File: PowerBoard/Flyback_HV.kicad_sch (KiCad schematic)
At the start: 43 parts, among them J3 Molex Microfit 3.0, Q2 FDD86250-F085, Q3 FGH75T65SQD-F155, T1 DA2034, U2 LT3750, U4 MCP14A0454-E/SN

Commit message: auto discharge circuit
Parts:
- removed D1: D, bots:D_SMB, symbol Device:D
- removed D3 (x2): D_Schottky, bots:D_SMC, symbol Device:D_Schottky
- removed D4 (x2): D_Zener, bots:D_SMA, symbol Device:D_Zener
- removed Q3 (x2): FGH75T65SQD-F155, bots:TO-247-3_Horizontal_TabDown, symbol Transistor_IGBT:IRG4PF50W
- added C1: 0.1u, bots:C_1210_3225Metric, symbol Device:C
- added D1, D10: SMAJ14A, bots:D_SMA, symbol bots:SMAJ14A
- added D11, D2: MUR860J, bots:D_SMC, symbol bots:MUR860J
- added D12: 3SMBJ5929B-TP, bots:D_SMB, symbol bots:D_ZENER_3SMBJ5929B-TP
- added D3: D_Schottky, bots:D_SMB, symbol Device:D_Schottky
- added Q3, Q7: FGH50T65SQD-F155, bots:TO-247-3_Horizontal_TabDown, symbol bots:FGH50T65SQD-F155
- added Q5: TN2130K1-G, BSS138:SOT95P240X111-3N, symbol bots:TN2130K1-G
- added Q6: STD11N60DM2, bots:DPAK-3_ONS, symbol bots:STD11N60DM2
- added R44: 1k 50W, bots:TO-263-2, symbol bots:1k 50W
- added R9: 100k, bots:R_0603_1608Metric, symbol Device:R
- added R9: 270k, bots:R_0603_1608Metric, symbol Device:R
- added R9 (x2): 5.1M, bots:R_0603_1608Metric, symbol Device:R
- added TP19: DONE, bots:TestPoint_Pad_1.0x1.0mm, symbol Connector:TestPoint
- added TP20: CHARGE, bots:TestPoint_Pad_1.0x1.0mm, symbol Connector:TestPoint
- added TP21: VGATE, bots:TestPoint_Pad_1.0x1.0mm, symbol Connector:TestPoint
- added TP22: GATEB, bots:TestPoint_Pad_1.0x1.0mm, symbol Connector:TestPoint
- added TP23: CHICKER_GATE, bots:TestPoint_Pad_1.0x1.0mm, symbol Connector:TestPoint
- added TP24: CHIP, bots:TestPoint_Pad_1.0x1.0mm, symbol Connector:TestPoint
- added TP25: CHICK, bots:TestPoint_Pad_1.0x1.0mm, symbol Connector:TestPoint
- U4: footprint bots:SOIC-8_3.9x4.9mm_P1.27mm -> SOIC8_SN_MCH
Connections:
- net CHARGE: now also TP20.1
- net CHICKER: now also TP25.1
- net CHICKER_GATE: now also TP23.1
- net CHICKER_HV: now also D11.2 (A), Q3.2 (C)
- net CHIP_EXTRA: now also TP24.1
- net DONE: now also TP19.1
- net EXTRA_GATE: now also TP22.1
- net EXTRA_HV: now also D2.2 (A), Q7.2 (C)
- net GNDPWR: now also C1.2, D1.2 (A), D10.2 (A), D12.2 (A), Q3.3 (E), Q5.2, Q6.3 (S), Q7.3 (E), R44.2, R9.2
- net HV: now also C1.1, D11.1 (K), D2.1 (K), D3.1 (K), R44.1, R9.1
- net HV_DIO: now also D3.2 (A)
- net IGBTGATE_CHICKER: now also D1.1 (K), Q3.1 (G)
- net IGBTGATE_EXTRA: now also D10.1 (K), Q7.1 (G)
- net VCC: now also R9.1
- net at Q2.1 (G), U2.7 (GATE): now also TP21.1
- new net AD_50W: Q6.2 (D), R44.3
- new net AD_G: D12.1 (K), Q5.3, Q6.1 (G), R9.2
- new net AD_LV_G: Q5.1, R9.1, R9.2
- new net AD_R: R9.1, R9.2
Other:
- note added: "Vth = 2.4V, at lowest 14.8 roughly this is still at 4V. So only when it is disconnected will it not be tied to ground"
- note removed: "4775.207283"
- note removed: "4797.333031"
- note removed: "7087.375394"
- moved on the sheet: C5, C6, D2, R6, R7, R8

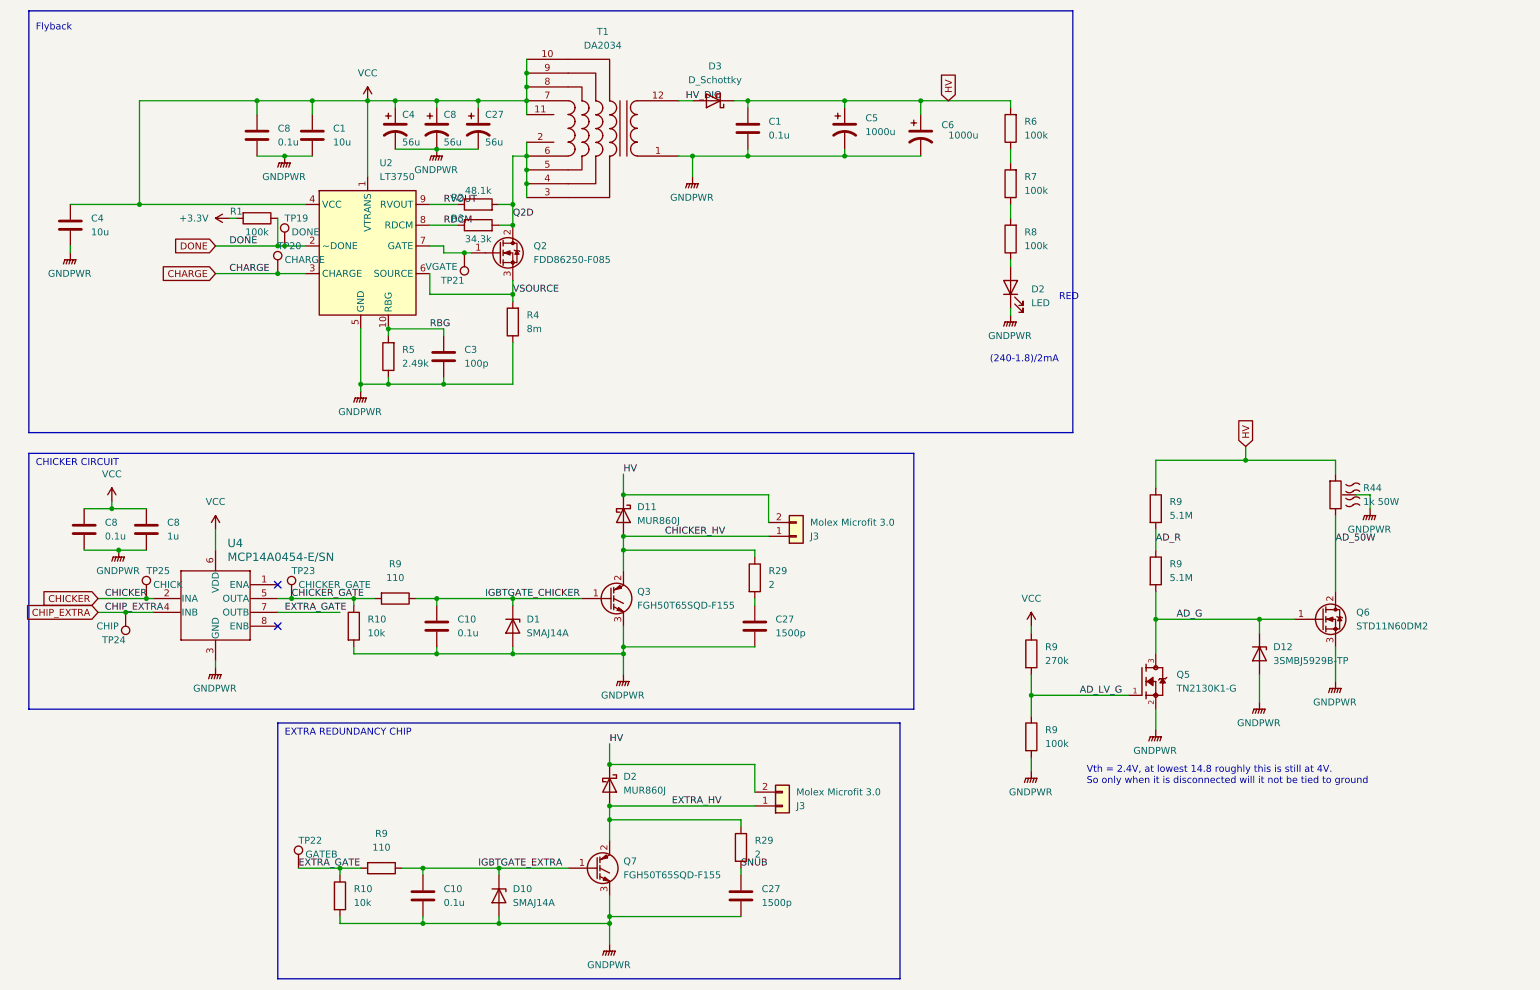
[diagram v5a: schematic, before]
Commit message: updated board edge clearance and cap model
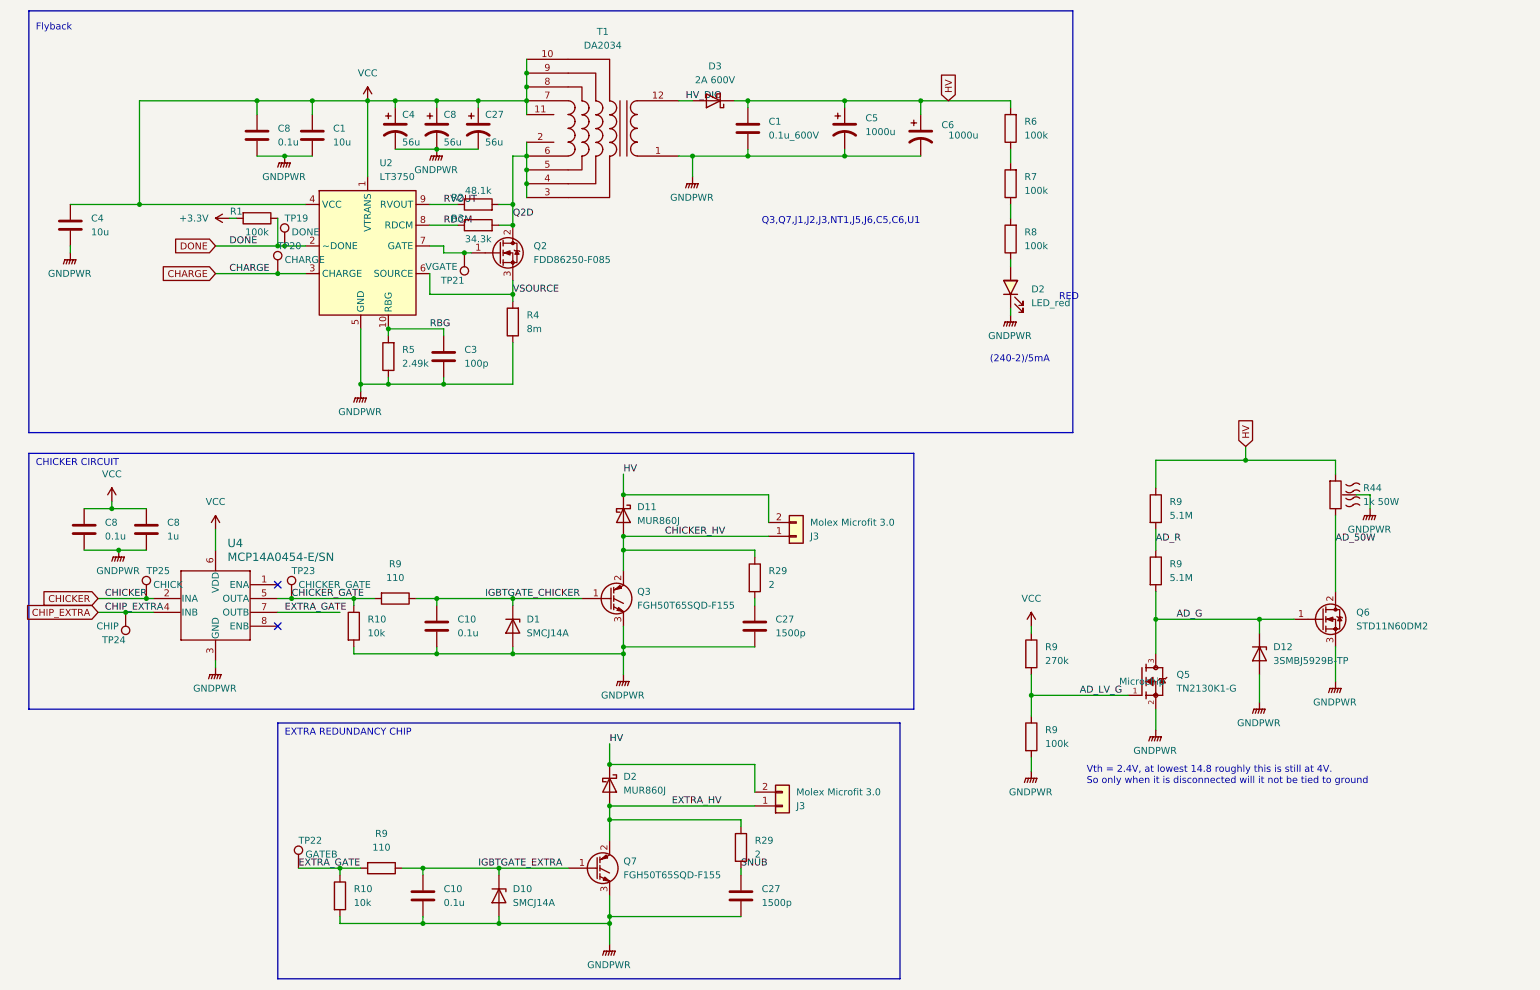
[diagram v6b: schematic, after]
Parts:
- removed D1, D10: SMAJ14A, bots:D_SMA, symbol bots:SMAJ14A
- added D1, D10: SMCJ14A, bots:D_SMC, symbol bots:SMCJ14A
- C1, C4: symbol Device:C -> bots:C_10u; JLC (none) -> 0805; LCSC (none) -> C440198; MPN (none) -> GRM21BR61H106KE43L; Manufacturer (none) -> Murata; Price (none) -> 0.0645
- C1: value 0.1u -> 0.1u_600V; symbol Device:C -> bots:C_0.1u_600V; JLC (none) -> 1210; LCSC (none) -> C342668; MPN (none) -> C3225X7T2J104KT000N; Manufacturer (none) -> TDK; Price (none) -> 0.3623
- C10, C8: symbol Device:C -> bots:C_0.1u; JLC (none) -> 0603; LCSC (none) -> C14663; MPN (none) -> CC0603KRX7R9BB104; Manufacturer (none) -> YAGEO; Price (none) -> 0.0021
- C27: symbol Device:C -> bots:C_1500p; JLC (none) -> 0805; LCSC (none) -> C342996; MPN (none) -> C2012C0G2A152JT000N; Manufacturer (none) -> TDK; Price (none) -> 0.0396
- C27, C4, C8: symbol bots:CAP_A768EB566M1VLAE042 -> bots:CAP_56uPOL; MPN (none) -> UWD1V560MCL1GS; Manufacturer (none) -> Nichion; Price (none) -> 0.79
- C3: symbol Device:C -> bots:C_100p; JLC (none) -> 0603; LCSC (none) -> C14858; MPN (none) -> CL10C101JB8NNNC; Manufacturer (none) -> Samsung Electro-Mechanics; Price (none) -> 0.0026
- C5: symbol Device:C_Polarized_US -> bots:C_1000u_POL; MPN (none) -> ESMQ251VSN102MQ45S; Manufacturer (none) -> Chemi-Con; Price (none) -> 9.07
- C6: symbol Device:C_Polarized_US -> bots:C_1000u_POL_reversed; MPN (none) -> ESMQ251VSN102MQ45S; Manufacturer (none) -> Chemi-Con; Price (none) -> 9.07
- C8: symbol Device:C -> bots:C_1u; JLC (none) -> 0603; LCSC (none) -> C15849; MPN (none) -> CL10A105KB8NNNC; Manufacturer (none) -> Samsung Electro-Mechanics; Price (none) -> 0.0046
- D11, D2: MPN (none) -> MUR860J; Manufacturer (none) -> WeEn Semiconductors; Price (none) -> 0.76
- D12: MPN (none) -> 3SMBJ5929B-TP; Manufacturer (none) -> Micro Commercial Co; Price (none) -> 0.63
- D2: value LED -> LED_red; symbol Device:LED -> bots:LED_red; JLC (none) -> SMD,1.5x3.2mm; LCSC (none) -> C2908310; MPN (none) -> RF-RUT112TS-BD; Manufacturer (none) -> Refond; Price (none) -> 0.1023
- D3: value D_Schottky -> 2A 600V; symbol Device:D_Schottky -> bots:MURS160-E3/52T; JLC (none) -> SMB(DO-214AA); LCSC (none) -> C59627; MPN (none) -> MURS160-E3/52T; Manufacturer (none) -> Vishay Intertech; Price (none) -> 0.1038
- J3: symbol Connector_Generic:Conn_01x02 -> bots:Molex_Microfit_3.0_1x2; MPN (none) -> 0436500215; Manufacturer (none) -> Molex; Price (none) -> 0.97
- Q2: JLC (none) -> TO-252; LCSC (none) -> C605020; MPN (none) -> FDD86250-F085; Manufacturer (none) -> onsemi; Price (none) -> 3.18
- Q3, Q7: JLC (none) -> TO-247; LCSC (none) -> C132704; MPN (none) -> FGH50T65SQD-F155; Manufacturer (none) -> onsemi; Price (none) -> 3.4798
- Q5: footprint BSS138:SOT95P240X111-3N -> bots:SOT95P240X111-3N; AVAILABILITY In Stock -> (none); Availability In Stock -> (none); Check_prices https://www.snapeda.com/parts/BSS138/Diodes+Inc./view-part/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 -> (none); DESCRIPTION N-Channel 50 V 200mA (Ta) 225mW (Ta) Surface Mount SOT-23-3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 -> (none); JLC (none) -> SOT-23-3; LCSC (none) -> C626652; MF Diodes Inc. -> (none); MP BSS138 -> (none); MPN (none) -> TN2130K1-G; Manufacturer (none) -> Microchip; PACKAGE SOT-23 ON -> (none); PRICE None -> (none); Package SOT-23-3 Diodes Inc. -> SOT-23-3; Price None -> 0.67; SnapEDA_Link https://www.snapeda.com/parts/BSS138/Diodes+Inc./view-part/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 -> (none)
- Q6: JLC (none) -> TO-252; LCSC (none) -> C2688635; MPN (none) -> STD11N60DM2; Manufacturer (none) -> STMicroelectronics; Price (none) -> 0.8474
- R1, R6, R7, R8, R9: symbol Device:R -> bots:R_100k; JLC (none) -> 0603; LCSC (none) -> C25803; MPN (none) -> 0603WAF1003T5E; Manufacturer (none) -> UNI-ROYAL(Uniroyal Elec); Price (none) -> 0.0009
- R10: symbol Device:R -> bots:R_10k; JLC (none) -> 0603; LCSC (none) -> C25804; MPN (none) -> 0603WAF1002T5E; Manufacturer (none) -> UNI-ROYAL(Uniroyal Elec); Price (none) -> 0.0008
- R2: symbol Device:R -> bots:R_47.5k; JLC (none) -> 0603; LCSC (none) -> C23061; MPN (none) -> 0603WAF4752T5E; Manufacturer (none) -> UNI-ROYAL(Uniroyal Elec); Price (none) -> 0.0009
- R29: symbol Device:R -> bots:R_2R_0805; JLC (none) -> 0805; LCSC (none) -> C17606; MPN (none) -> 0805W8F200KT5E; Manufacturer (none) -> UNI-ROYAL(Uniroyal Elec); Price (none) -> 0.0025
- R3: symbol Device:R -> bots:R_34k; JLC (none) -> 0603; LCSC (none) -> C23008; MPN (none) -> 0603WAF3402T5E; Manufacturer (none) -> UNI-ROYAL(Uniroyal Elec); Price (none) -> 0.001
- R4: symbol Device:R -> bots:R_8m; JLC (none) -> 1206; LCSC (none) -> C326567; MPN (none) -> PE1206FRF470R008L; Manufacturer (none) -> YAGEO; Price (none) -> 0.0695
- R44: MPN (none) -> TDH50H1K00FE-TR; Manufacturer (none) -> Ohmite; Price (none) -> 10.65
- R5: symbol Device:R -> bots:R_2.49k; JLC (none) -> 0603; LCSC (none) -> C108190; MPN (none) -> RC0603FR-072K49L; Manufacturer (none) -> YAGEO; Price (none) -> 0.001
- R9: symbol Device:R -> bots:R_270k; JLC (none) -> 0603; LCSC (none) -> C22965; MPN (none) -> 0603WAF2703T5E; Manufacturer (none) -> UNI-ROYAL(Uniroyal Elec); Price (none) -> 0.0009
- R9: symbol Device:R -> bots:R_110R; JLC (none) -> 0603; LCSC (none) -> C22781; MPN (none) -> 0603WAF1100T5E; Manufacturer (none) -> UNI-ROYAL(Uniroyal Elec); Price (none) -> 0.001
- R9: symbol Device:R -> bots:R_5.1M; JLC (none) -> 0603; LCSC (none) -> C322178; MPN (none) -> RS-03L5104FT; Manufacturer (none) -> FH (Guangdong Fenghua Advanced Tech); Price (none) -> 0.0013
- T1: MPN (none) -> DA2034-ALD; Manufacturer (none) -> Coilcraft; Price (none) -> 13.35
- TP19, TP20, TP21, TP22, TP23, TP24, TP25: symbol Connector:TestPoint -> bots:TestPoint_1x1; now left out of the parts list
- U2: JLC (none) -> MSOP-10; LCSC (none) -> C84289; MPN (none) -> LT3750EMS#PBF; Manufacturer (none) -> Analog Devices; Price (none) -> 15.73
- U4: footprint SOIC8_SN_MCH -> bots:SOIC-8_3.9x4.9mm_P1.27mm; MPN (none) -> MCP14A0454-E/SN; Manufacturer (none) -> Microchip; Price (none) -> 2.42
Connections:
- net GNDPWR: now also D1.2 (A), D10.2 (A)
- net IGBTGATE_CHICKER: now also D1.1 (K)
- net IGBTGATE_EXTRA: now also D10.1 (K)
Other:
- note added: "(240-2)/5mA"
- note added: "Q3,Q7,J1,J2,J3,NT1,J5,J6,C5,C6,U1"
- note removed: "(240-1.8)/2mA"

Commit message: updated fuse, pillars, caps
- Added 10A fuse to VCC pillar
- Added CANL pillar next to CANH (and old CANL pillar is NC)
- Adjusted CAPS left and right by 1mm to add space for the board
- Added another LED wired to the RP2040 for CAN status
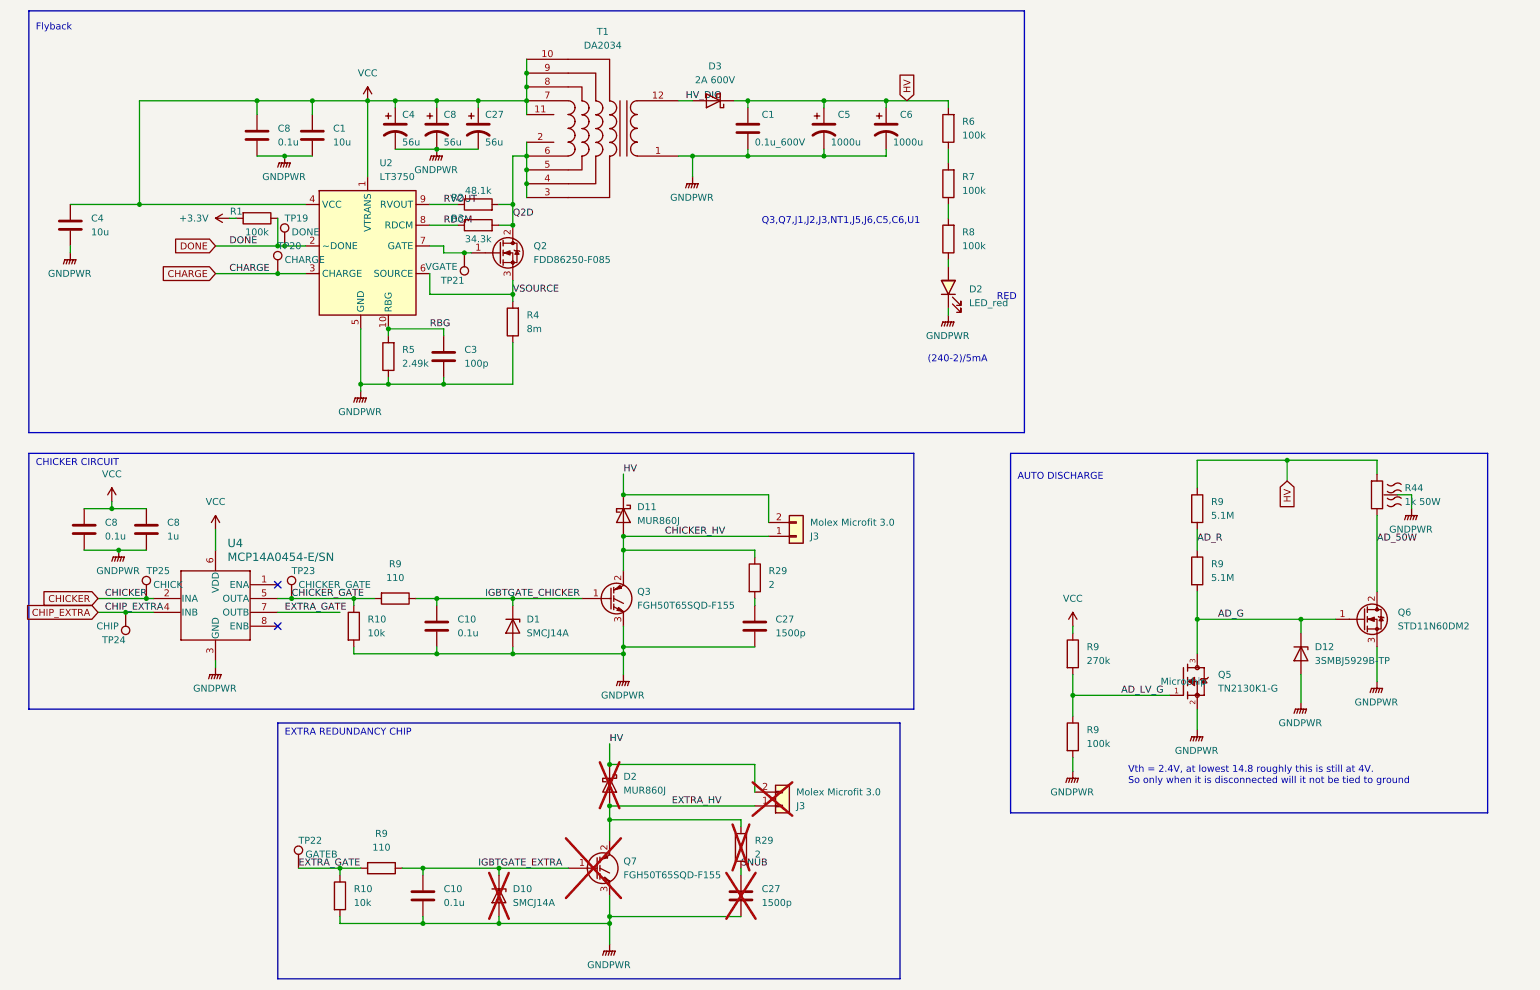
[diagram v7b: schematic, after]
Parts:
- C27, D10, D2, J3, Q7, R29: now not fitted
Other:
- note added: "AUTO DISCHARGE"
- moved on the sheet: C5, C6, D12, D2, Q5, Q6, R44, R6, R7, R8, R9

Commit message: modified design
- added RCD snubber on transformer primary
- moved GND and CANL CANH posts to make room (and next to eachother)
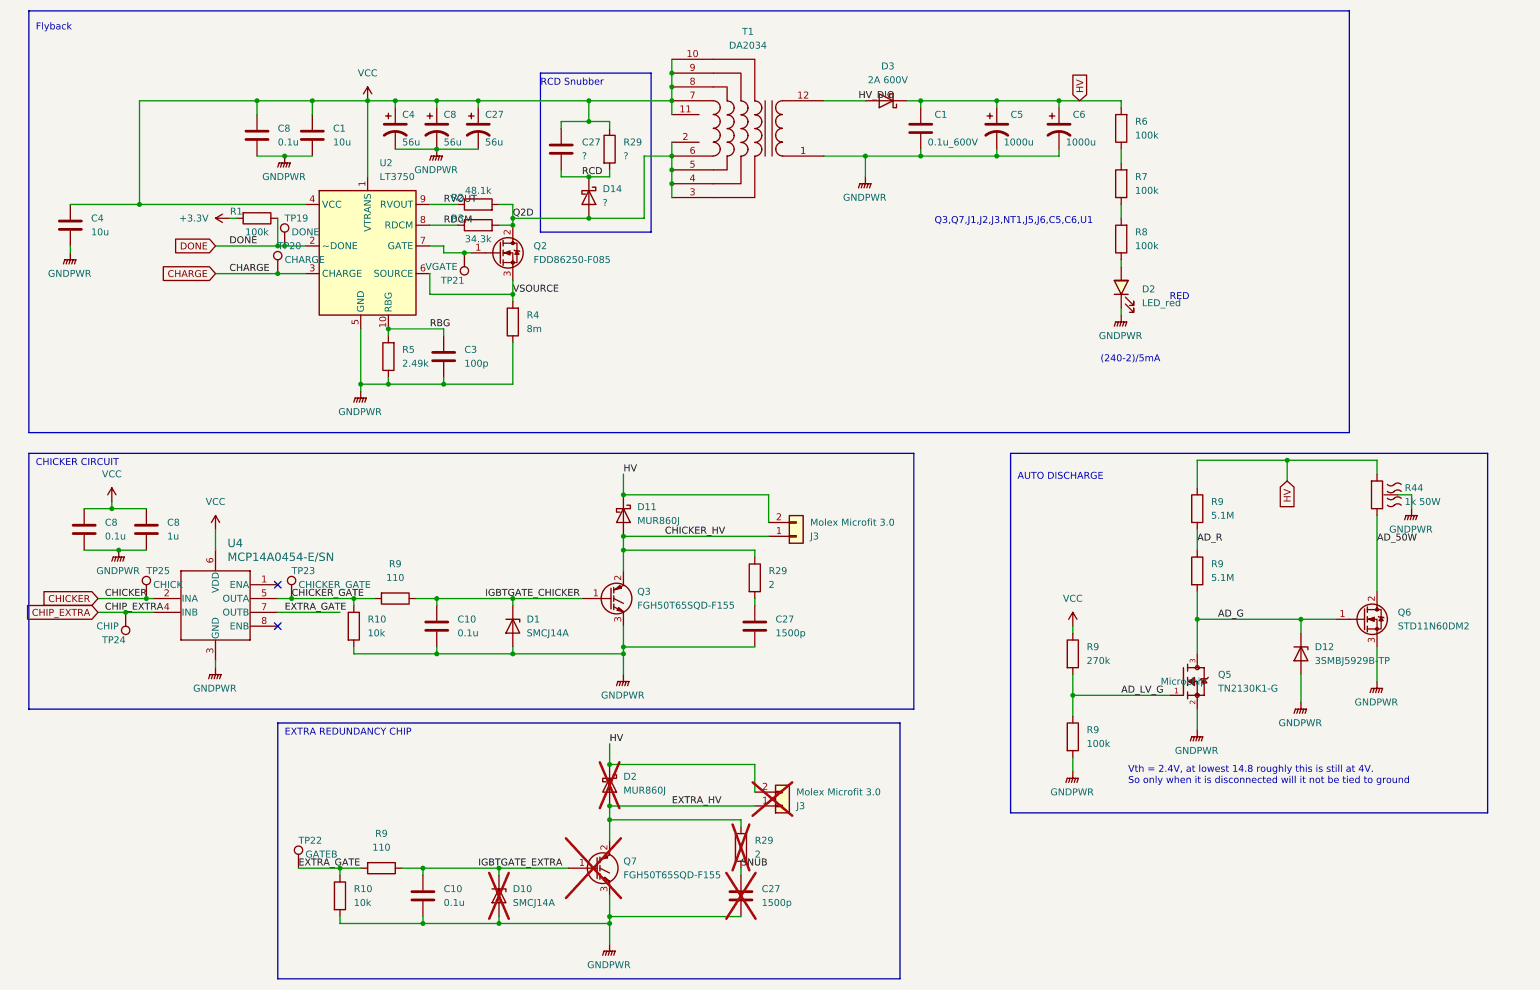
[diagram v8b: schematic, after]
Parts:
- added C27: ?, bots:C_0805_2012Metric, symbol bots:C_1500p
- added D14: ?, bots:D_SMA, symbol bots:MURS160-E3/52T
- added R29: ?, bots:R_0805_2012Metric, symbol bots:R_2R_0805
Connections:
- net Q2D: now also D14.2 (A)
- net VCC: now also C27.1, R29.1
- new net RCD: C27.2, D14.1 (K), R29.2
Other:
- note added: "RCD Snubber"
- moved on the sheet: C1, C5, C6, D2, D3, R6, R7, R8, T1
